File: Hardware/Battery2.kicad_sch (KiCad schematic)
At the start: 68 parts

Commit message: Bms plug and play, 2nd iteration with the same pinout
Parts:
- removed R126, R127, R128, R129, R130, R131, R132, R133, R134, R135, R136, R137, R138, R139: 10, footrpint:RESC6331X80N, symbol Device:R_Small
- added F22, F23, F24, F25, F26, F27, F28, F29, F30, F31, F32, F33, F34, F35, F36, F37: 400mA, Fuse:Fuse_0805_2012Metric, symbol Device:Fuse_Small
- added R77, R78, R79, R80, R81, R82, R83, R84, R85, R86, R87, R88, R89, R90: 20R 2W, Resistor_SMD:R_2512_6332Metric, symbol Device:R_Small
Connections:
- net CB0: now also R90.2
- net CB1: now also R89.2
- net CB10: now also R80.2
- net CB11: now also R79.2
- net CB12: now also R78.2
- net CB13: now also R77.2
- net CB2: now also R88.2
- net CB3: now also R87.2
- net CB4: now also R86.2
- net CB5: now also R85.2
- net CB6: now also R84.2
- net CB7: now also R83.2
- net CB8: now also R82.2
- net CB9: now also R81.2
- net CELL14: now also F36.1; no longer R125.1
- net CELL15: now also F35.1; no longer R124.1
- net CELL16: now also F34.1; no longer R123.1
- net CELL17: now also F33.1; no longer R122.1
- net CELL18: now also F32.1; no longer R121.1
- net CELL19: now also F31.1; no longer R120.1
- net CELL20: now also F30.1; no longer R119.1
- net CELL21: now also F29.1; no longer R118.1
- net CELL22: now also F28.1; no longer R117.1
- net CELL23: now also F27.1; no longer R116.1
- net CELL24: now also F26.1; no longer R115.1
- net CELL25: now also F25.1; no longer R114.1
- net CELL26: now also F23.1, F24.1; no longer R113.1
- net GND_HV2: now also F22.2; no longer BT26.2 (-), R112.1
- new net: F35.2, R124.1, R88.1
- new net: F29.2, R118.1, R82.1
- new net: F27.2, R116.1, R80.1
- new net: F34.2, R123.1, R87.1
- new net: F25.2, R114.1, R78.1
- new net: F30.2, R119.1, R83.1
- new net: F26.2, R115.1, R79.1
- new net: F31.2, R120.1, R84.1
- new net: F24.2, R113.1, R77.1
- new net: F32.2, R121.1, R85.1
- new net: F36.2, R125.1, R89.1
- new net: F37.2, R112.1, R90.1
- new net: F28.2, R117.1, R81.1
- new net: F33.2, R122.1, R86.1
- new net Batt2_+: F23.2
- new net Batt_Coupling: BT26.2 (-), F22.1, F37.1
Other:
- moved on the sheet: BT14, BT15, BT16, BT17, BT18, BT19, BT20, BT21, BT22, BT23, BT24, BT25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

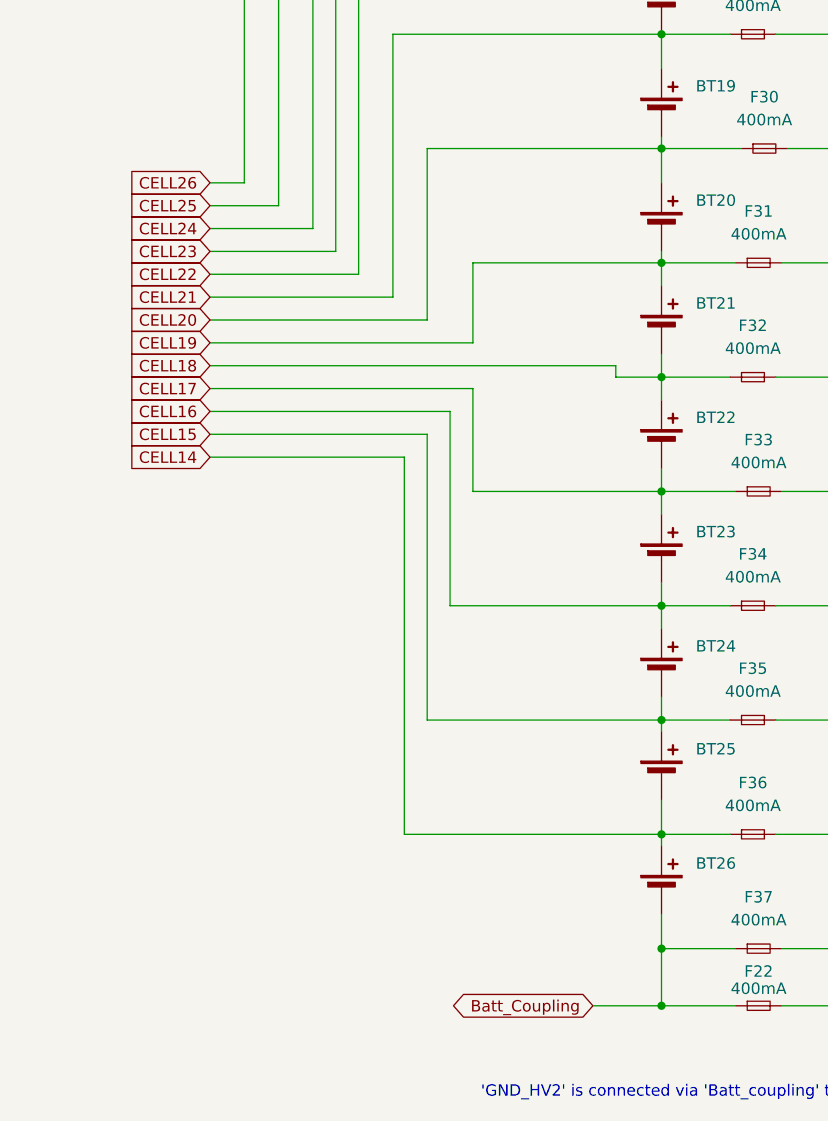
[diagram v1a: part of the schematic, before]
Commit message: New connectors jst_xh for low voltage side of bms
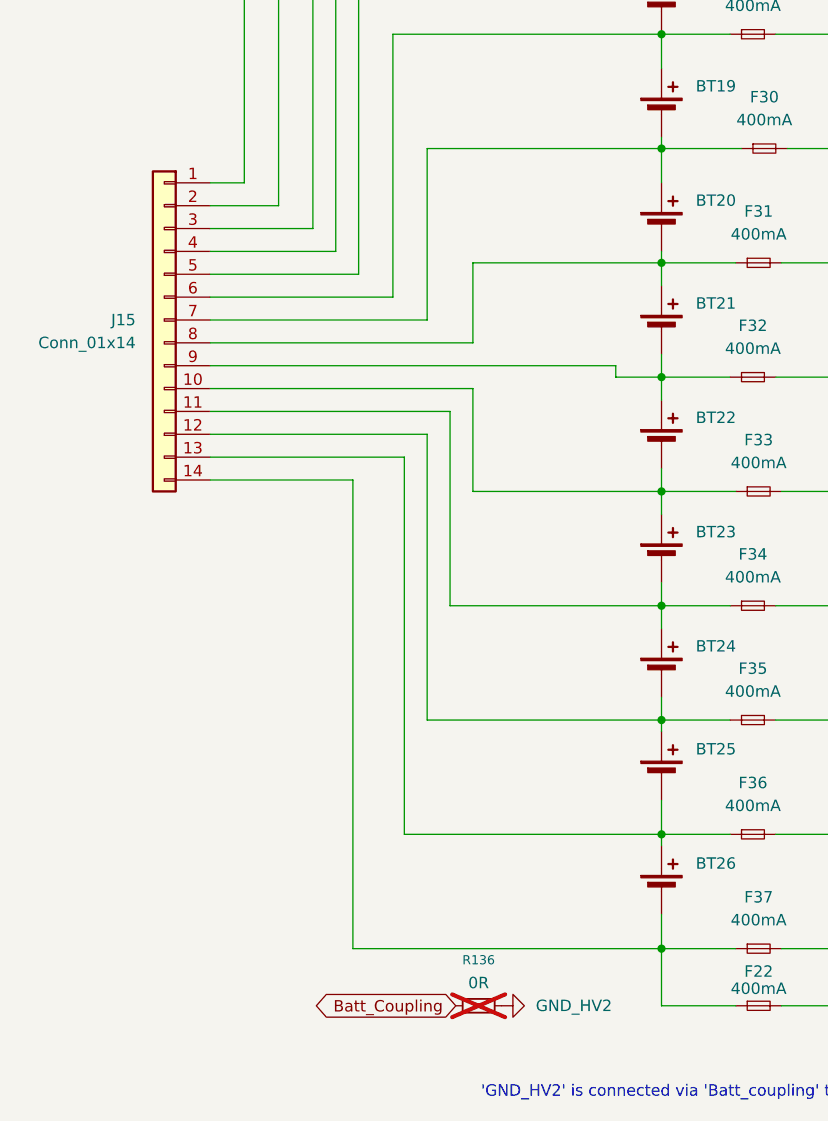
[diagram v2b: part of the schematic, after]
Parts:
- added J15: Conn_01x14, Connector_JST:JST_XH_S14B-XH-A_1x14_P2.50mm_Horizontal, symbol Connector_Generic:Conn_01x14
- added R136: 0R, Resistor_SMD:R_1206_3216Metric, symbol Device:R_Small
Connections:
- net Batt_Coupling: now also R136.1; no longer BT26.2 (-), F22.1, F37.1
- net GND_HV2: now also R136.2
- net CELL14: no longer names the net of BT25.2 (-), BT26.1 (+), F36.1
- net CELL14: now also J15.13 (Pin_13)
- net CELL15: no longer names the net of BT24.2 (-), BT25.1 (+), F35.1
- net CELL15: now also J15.12 (Pin_12)
- net CELL16: no longer names the net of BT23.2 (-), BT24.1 (+), F34.1
- net CELL16: now also J15.11 (Pin_11)
- net CELL17: no longer names the net of BT22.2 (-), BT23.1 (+), F33.1
- net CELL17: now also J15.10 (Pin_10)
- net CELL18: no longer names the net of BT21.2 (-), BT22.1 (+), F32.1
- net CELL18: now also J15.9 (Pin_9)
- net CELL19: no longer names the net of BT20.2 (-), BT21.1 (+), F31.1
- net CELL19: now also J15.8 (Pin_8)
- net CELL20: no longer names the net of BT19.2 (-), BT20.1 (+), F30.1
- net CELL20: now also J15.7 (Pin_7)
- net CELL21: no longer names the net of BT18.2 (-), BT19.1 (+), F29.1
- net CELL21: now also J15.6 (Pin_6)
- net CELL22: no longer names the net of BT17.2 (-), BT18.1 (+), F28.1
- net CELL22: now also J15.5 (Pin_5)
- net CELL23: no longer names the net of BT16.2 (-), BT17.1 (+), F27.1
- net CELL23: now also J15.4 (Pin_4)
- net CELL24: no longer names the net of BT15.2 (-), BT16.1 (+), F26.1
- net CELL24: now also J15.3 (Pin_3)
- net CELL25: no longer names the net of BT14.2 (-), BT15.1 (+), F25.1
- net CELL25: now also J15.2 (Pin_2)
- net CELL26 renamed Stack+
- net Stack+: now also J15.1 (Pin_1)
- new net: BT26.2 (-), F22.1, F37.1, J15.14 (Pin_14)
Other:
- title: (none) -> Battery Management System for a high power gokart battery

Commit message: No drc errors
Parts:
- removed R136: 0R, Resistor_SMD:R_1206_3216Metric, symbol Device:R_Small
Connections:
- net Stack-: now reaches BT26.2 (-), F22.1, F37.1, J15.14 (Pin_14)
- net Stack+: no longer names the net of BT14.1 (+), F23.1, F24.1, J15.1 (Pin_1)
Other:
- note removed: "'GND_HV2' is connected via 'Batt_coupling' to cell number 13 and serves as a ground for 2nd ltc"
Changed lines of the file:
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@@
 		)
 	)
-	(text "'GND_HV2' is connected via 'Batt_coupling' to cell number 13 and serves as a ground for 2nd ltc"
-		(exclude_from_sim no)
-		(at 97.536 203.962 0)
-		(effects
-			(font
-				(size 1.27 1.27)
-			)
-		)
-	)
 	(text "Batteries in the schematic are there only for \nprinciple,they are ment to show how the pcb \nis connected to the battery pack. In reality\nthe connection is purely external as the\nconnector on the left shows. \n\n"
 		(exclude_from_sim no)
@@
 	)
 	(junction
-		(at 75.565 13.97)
-		(diameter 0)
-		(color 0 0 0 0)
-	)
-	(junction
 		(at 100.33 22.86)
 		(diameter 0)
@@
 	)
 	(junction
+		(at 75.565 194.31)
+		(diameter 0)
+		(color 0 0 0 0)
+	)
+	(junction
 		(at 75.565 111.76)
 		(diameter 0)
@@
 	(wire
 		(pts
-			(xy 83.82 76.2) (xy 75.565 76.2)
+			(xy 72.39 194.31) (xy 75.565 194.31)
 		)
 		(stroke
@@
 	(wire
 		(pts
-			(xy 41.91 113.03) (xy 25.4 113.03)
+			(xy 83.82 76.2) (xy 75.565 76.2)
 		)
 		(stroke
@@
 	(wire
 		(pts
-			(xy 102.87 146.05) (xy 102.87 149.86)
+			(xy 41.91 113.03) (xy 25.4 113.03)
 		)
 		(stroke
@@
 	(wire
 		(pts
-			(xy 83.185 162.56) (xy 75.565 162.56)
+			(xy 102.87 146.05) (xy 102.87 149.86)
 		)
 		(stroke
@@
 	(wire
 		(pts
-			(xy 113.03 86.36) (xy 114.3 86.36)
+			(xy 83.185 162.56) (xy 75.565 162.56)
 		)
 		(stroke
@@
 	(wire
 		(pts
-			(xy 75.565 13.97) (xy 66.675 13.97)
+			(xy 113.03 86.36) (xy 114.3 86.36)
 		)
 		(stroke
@@
 		)
 	)
-	(global_label "Batt_Coupling"
-		(shape bidirectional)
-		(at 52.705 194.31 180)
-		(fields_autoplaced yes)
-		(effects
-			(font
-				(size 1.27 1.27)
-			)
-			(justify right)
-		)
-		(property "Intersheetrefs" "${INTERSHEET_REFS}"
-			(at 35.4855 194.31 0)
-			(hide yes)
-			(show_name no)
-			(do_not_autoplace no)
-			(effects
-				(font
-					(size 1.27 1.27)
-				)
-				(justify right)
-			)
-		)
-	)
-	(global_label "Stack+"
+	(global_label "Stack-"
 		(shape input)
-		(at 66.675 13.97 180)
+		(at 72.39 194.31 180)
 		(fields_autoplaced yes)
 		(effects
@@
 		)
 		(property "Intersheetrefs" "${INTERSHEET_REFS}"
-			(at 56.9165 13.97 0)
+			(at 62.6315 194.31 0)
 			(hide yes)
 			(show_name no)
@@
 	)
 	(symbol
-		(lib_id "power:GND")
-		(at 57.785 194.31 90)
-		(unit 1)
-		(body_style 1)
-		(exclude_from_sim no)
-		(in_bom yes)
-		(on_board yes)
-		(in_pos_files yes)
-		(dnp no)
-		(property "Reference" "#PWR0113"
-			(at 64.135 194.31 0)
-			(hide yes)
-			(show_name no)
-			(do_not_autoplace no)
-			(effects
-				(font
-					(size 1.27 1.27)
-				)
-			)
-		)
-		(property "Value" "GND_HV2"
-			(at 61.595 194.31 90)
-			(show_name no)
-			(do_not_autoplace no)
-			(effects
-				(font
-					(size 1.27 1.27)
-				)
-				(justify right)
-			)
-		)
-		(property "Footprint" ""
-			(at 57.785 194.31 0)
-			(hide yes)
-			(show_name no)
-			(do_not_autoplace no)
-			(effects
-				(font
-					(size 1.27 1.27)
-				)
-			)
-		)
-		(property "Datasheet" ""
-			(at 57.785 194.31 0)
-			(hide yes)
-			(show_name no)
-			(do_not_autoplace no)
-			(effects
-				(font
-					(size 1.27 1.27)
-				)
-			)
-		)
-		(property "Description" "Power symbol creates a global label with name \"GND\" , ground"
-			(at 57.785 194.31 0)
-			(hide yes)
-			(show_name no)
-			(do_not_autoplace no)
-			(effects
-				(font
-					(size 1.27 1.27)
-				)
-			)
-		)
-		(pin "1"
-		)
-		(instances
-			(project "BMS"
-				(path "/26289bb6-56bc-4ca1-b1a2-18d58d1afdf5/99f7ea83-6836-44ea-889b-f0d453e84b38/3dcd8643-765f-4aab-99d6-4ed68d4de44f"
-					(reference "#PWR0113")
-					(unit 1)
-				)
-			)
-		)
-	)
-	(symbol
 		(lib_id "Device:C_Small")
 		(at 154.94 38.1 180)
@@
 					(unit 1)
 				)
-			)
-		)
-	)
-	(symbol
-		(lib_id "Device:R_Small")
-		(at 55.245 194.31 90)
-		(unit 1)
-		(body_style 1)
-		(exclude_from_sim no)
-		(in_bom yes)
-		(on_board yes)
-		(in_pos_files yes)
-		(dnp yes)
-		(fields_autoplaced yes)
-		(property "Reference" "R136"
-			(at 55.245 189.23 90)
-			(show_name no)
-			(do_not_autoplace no)
-			(effects
-				(font
-					(size 1.016 1.016)
-				)
-			)
-		)
-		(property "Value" "0R"
-			(at 55.245 191.77 90)
-			(show_name no)
-			(do_not_autoplace no)
-			(effects
-				(font
-					(size 1.27 1.27)
-				)
-			)
-		)
-		(property "Footprint" "Resistor_SMD:R_1206_3216Metric"
-			(at 55.245 194.31 0)
-			(hide yes)
-			(show_name no)
-			(do_not_autoplace no)
-			(effects
-				(font
-					(size 1.27 1.27)
-				)
-			)
-		)
-		(property "Datasheet" ""
-			(at 55.245 194.31 0)
-			(hide yes)
-			(show_name no)
-			(do_not_autoplace no)
-			(effects
-				(font
-					(size 1.27 1.27)
-				)
-			)
-		)
-		(property "Description" "Resistor, small symbol"
-			(at 55.245 194.31 0)
-			(hide yes)
-			(show_name no)
-			(do_not_autoplace no)
-			(effects
-				(font
-					(size 1.27 1.27)
-				)
-			)
-		)
-		(pin "2"
-		)
-		(pin "1"
-		)
-		(instances
-			(project "BMS"
-				(path "/26289bb6-56bc-4ca1-b1a2-18d58d1afdf5/99f7ea83-6836-44ea-889b-f0d453e84b38/3dcd8643-765f-4aab-99d6-4ed68d4de44f"
-					(reference "R136")
-					(unit 1)
-				)
